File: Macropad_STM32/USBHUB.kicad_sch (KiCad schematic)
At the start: 36 parts, among them J4 USB_C_Receptacle_USB2.0, J5 USB_C_Receptacle_USB2.0, J6 USB_C_Receptacle_USB2.0, U2 CY7C65632-28LTXCT, U4 USBLC6-2SC6, U5 USBLC6-2SC6, U6 USBLC6-2SC6, U7 USBLC6-2SC6, Y1 12MHz

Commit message: Schematic changes Motherboard nearing completion
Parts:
- removed C17, C18, C19: 100n, Capacitor_SMD:C_0805_2012Metric_Pad1.18x1.45mm_HandSolder, symbol Device:C
- removed F2: 500mA, Fuse:Fuse_1206_3216Metric_Pad1.42x1.75mm_HandSolder, symbol Device:Polyfuse
- removed FB1 (x2): 600R, Fuse:Fuse_0805_2012Metric_Pad1.15x1.40mm_HandSolder, symbol Device:FerriteBead_Small
- removed J4, J5: USB_C_Receptacle_USB2.0, Connector_USB:USB_C_Receptacle_HRO_TYPE-C-31-M-12, symbol Hub16-rescue:USB_C_Receptacle_USB2.0-Connector
- removed U4, U5: USBLC6-2SC6, Package_TO_SOT_SMD:SOT-23-6, symbol Hub16-rescue:USBLC6-2SC6-josh-ic
- added C18, C37, C59: 2u2, Capacitor_SMD:C_0805_2012Metric_Pad1.18x1.45mm_HandSolder, symbol Device:C_Small
- added C19, C61, C62: 100u, Capacitor_SMD:C_Elec_6.3x5.4, symbol Device:C_Polarized
- added F5: 500mA, Fuse:Fuse_1206_3216Metric_Pad1.42x1.75mm_HandSolder, symbol Device:Polyfuse
- added FB1 (x2): 120R, Fuse:Fuse_0805_2012Metric_Pad1.15x1.40mm_HandSolder, symbol Device:FerriteBead_Small
- added J13, J14, J17, J18, J19, J5: Conn_01x04_Socket, Connector_PinHeader_2.54mm:PinHeader_1x04_P2.54mm_Vertical, symbol Connector:Conn_01x04_Socket
- added J15, J20: USB_C_Receptacle_USB2.0, Connector_USB:USB_C_Receptacle_HRO_TYPE-C-31-M-12, symbol Hub16-rescue:USB_C_Receptacle_USB2.0-Connector
- added U8: USBLC6-2SC6, Package_TO_SOT_SMD:SOT-23-6, symbol Hub16-rescue:USBLC6-2SC6-josh-ic
- FB1: value 600R -> 120R
- R10, R11, R8, R9: now not fitted
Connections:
- net +5V: now also J13.1 (Pin_1), J18.1 (Pin_1), J5.1 (Pin_1); no longer FB1.2
- net D1_D+: now also J18.3 (Pin_3), J19.3 (Pin_3), U8.4 (IO2)
- net D1_D-: now also J18.2 (Pin_2), J19.2 (Pin_2), U8.6 (IO1)
- net D2_D+: now also J17.3 (Pin_3), J5.3 (Pin_3)
- net D2_D-: now also J17.2 (Pin_2), J5.2 (Pin_2)
- net D3_D+: now also J13.3 (Pin_3), J14.3 (Pin_3)
- net D3_D-: now also J13.2 (Pin_2), J14.2 (Pin_2)
- net GND: now also C18.2, C19.2, C37.2, C59.2, C61.2, C62.2, J13.4 (Pin_4), J18.4 (Pin_4), J5.4 (Pin_4); no longer J6.A1 (GND), J6.A12 (GND), J6.B1 (GND), J6.B12 (GND), J6.S1 (SHIELD), U6.2 (GND), U7.2 (GND)
- net D3_VBUS: now reaches F4.1, J6.A4 (VBUS), J6.A9 (VBUS), J6.B4 (VBUS), J6.B9 (VBUS), U7.5 (VBUS)
- net at F4.2, FB1.1: now also C62.1
- net at U6.1 (IO1): now also J15.A7 (D-), J15.B7 (D-)
- net at U6.3 (IO2): now also J15.A6 (D+), J15.B6 (D+)
- net D1_VBUS: now reaches F3.1
- net D1_VBUS: now also J20.A4 (VBUS), J20.A9 (VBUS), J20.B4 (VBUS), J20.B9 (VBUS), U8.5 (VBUS); no longer U6.5 (VBUS)
- net at F3.2: now also C61.1, FB1.1
- new net: C19.1, F5.2, FB1.1
- new net: C18.1, FB1.2, J17.1 (Pin_1)
- new net: C59.1, FB1.2, J14.1 (Pin_1)
- new net: J20.A6 (D+), J20.B6 (D+), U8.3 (IO2)
- new net: J20.A7 (D-), J20.B7 (D-), U8.1 (IO1)
- new net: C37.1, FB1.2, J19.1 (Pin_1)
- new net D1_GND: J19.4 (Pin_4), J20.A1 (GND), J20.A12 (GND), J20.B1 (GND), J20.B12 (GND), J20.S1 (SHIELD), U8.2 (GND)
- new net D2_GND: J15.A1 (GND), J15.A12 (GND), J15.B1 (GND), J15.B12 (GND), J15.S1 (SHIELD), J17.4 (Pin_4), U6.2 (GND)
- new net D2_VBUS: F5.1, J15.A4 (VBUS), J15.A9 (VBUS), J15.B4 (VBUS), J15.B9 (VBUS), U6.5 (VBUS)
- new net D3_GND: J14.4 (Pin_4), J6.A1 (GND), J6.A12 (GND), J6.B1 (GND), J6.B12 (GND), J6.S1 (SHIELD), U7.2 (GND)
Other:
- company: (none) -> Irfaan
- title: (none) -> STM32 Macropad
- moved on the sheet: C27, C28, F4, FB1, JP2, R12, R13, U2, U7, Y1

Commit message: Revision 1 nearly finished
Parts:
- removed J15, J20: USB_C_Receptacle_USB2.0, Connector_USB:USB_C_Receptacle_HRO_TYPE-C-31-M-12, symbol Hub16-rescue:USB_C_Receptacle_USB2.0-Connector
- added J2, J8: USB_A, SK6812SIDE:AMPHENOL_UE27AC54100, symbol Connector:USB_A
- J13, J14, J17, J18, J19, J5: footprint Connector_PinHeader_2.54mm:PinHeader_1x04_P2.54mm_Vertical -> SK6812SIDE:MOLEX_0781710004
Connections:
- net +3V3 is gone; now on net +3.3V: C27.1, C28.1
- net D1_D+: no longer J19.3 (Pin_3), U8.4 (IO2)
- net D1_D-: no longer J19.2 (Pin_2), U8.6 (IO1)
- net D1_GND: now also C37.2, C61.2, J2.4 (GND), J2.5 (Shield)
- net D1_VBUS: now also J2.1 (VBUS)
- net D2_D+: no longer J17.3 (Pin_3), U6.4 (IO2)
- net D2_D-: no longer J17.2 (Pin_2), U6.6 (IO1)
- net D2_GND: now also C18.2, C19.2, J8.4 (GND), J8.5 (Shield)
- net D2_VBUS: now also J8.1 (VBUS)
- net D3_D+: no longer J14.3 (Pin_3), U7.4 (IO2)
- net D3_D-: no longer J14.2 (Pin_2), U7.6 (IO1)
- net D3_GND: now also C59.2, C62.2
- net GND: no longer C18.2, C19.2, C37.2, C59.2, C61.2, C62.2
- net at U8.3 (IO2): now also J2.3 (D+)
- net at U8.1 (IO1): now also J2.2 (D-)
- net at U6.1 (IO1): now also J8.2 (D-)
- net at U6.3 (IO2): now also J8.3 (D+)
- new net Daughter_D1_D+: J19.3 (Pin_3), U8.4 (IO2)
- new net Daughter_D1_D-: J19.2 (Pin_2), U8.6 (IO1)
- new net Daughter_D2_D+: J17.3 (Pin_3), U6.4 (IO2)
- new net Daughter_D2_D-: J17.2 (Pin_2), U6.6 (IO1)
- new net Daughter_D3_D+: J14.3 (Pin_3), U7.4 (IO2)
- new net Daughter_D3_D-: J14.2 (Pin_2), U7.6 (IO1)
- no-connect marks 15 -> 7

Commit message: Nearly finished Todo: - Fix silkscreen - Final check
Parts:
- removed J13, J14, J17, J18, J19, J5: Conn_01x04_Socket, SK6812SIDE:MOLEX_0781710004, symbol Connector:Conn_01x04_Socket
- JP2: footprint Connector_PinHeader_2.54mm:PinHeader_1x03_P2.54mm_Vertical -> Jumper:SolderJumper-3_P2.0mm_Open_TrianglePad1.0x1.5mm_NumberLabels
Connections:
- net D1_GND is gone; now on net GND: C37.2, C61.2, J2.4 (GND), J2.5 (Shield), U8.2 (GND)
- net D1_VBUS is gone; now on net +5V: F3.1, J2.1 (VBUS), U8.5 (VBUS)
- net D2_GND is gone; now on net GND: C18.2, C19.2, J8.4 (GND), J8.5 (Shield), U6.2 (GND)
- net D2_VBUS is gone; now on net +5V: F5.1, J8.1 (VBUS), U6.5 (VBUS)
- net D3_GND is gone; now on net GND: C59.2, C62.2, J6.A1 (GND), J6.A12 (GND), J6.B1 (GND), J6.B12 (GND), J6.S1 (SHIELD), U7.2 (GND)
- net D3_VBUS is gone; now on net +5V: F4.1, J6.A4 (VBUS), J6.A9 (VBUS), J6.B4 (VBUS), J6.B9 (VBUS), U7.5 (VBUS)
- net Daughter_D1_D+ is gone; now on net D2_D+: U8.4 (IO2)
- net Daughter_D1_D- is gone; now on net D2_D-: U8.6 (IO1)
- net Daughter_D2_D+ is gone; now on net D3_D+: U6.4 (IO2)
- net Daughter_D2_D- is gone; now on net D3_D-: U6.6 (IO1)
- net Daughter_D3_D+ is gone; now on net D1_D+: U7.4 (IO2)
- net Daughter_D3_D- is gone; now on net D1_D-: U7.6 (IO1)
- net +5V: now also C18.1, C37.1, C59.1, FB1.2, FB1.2, FB1.2

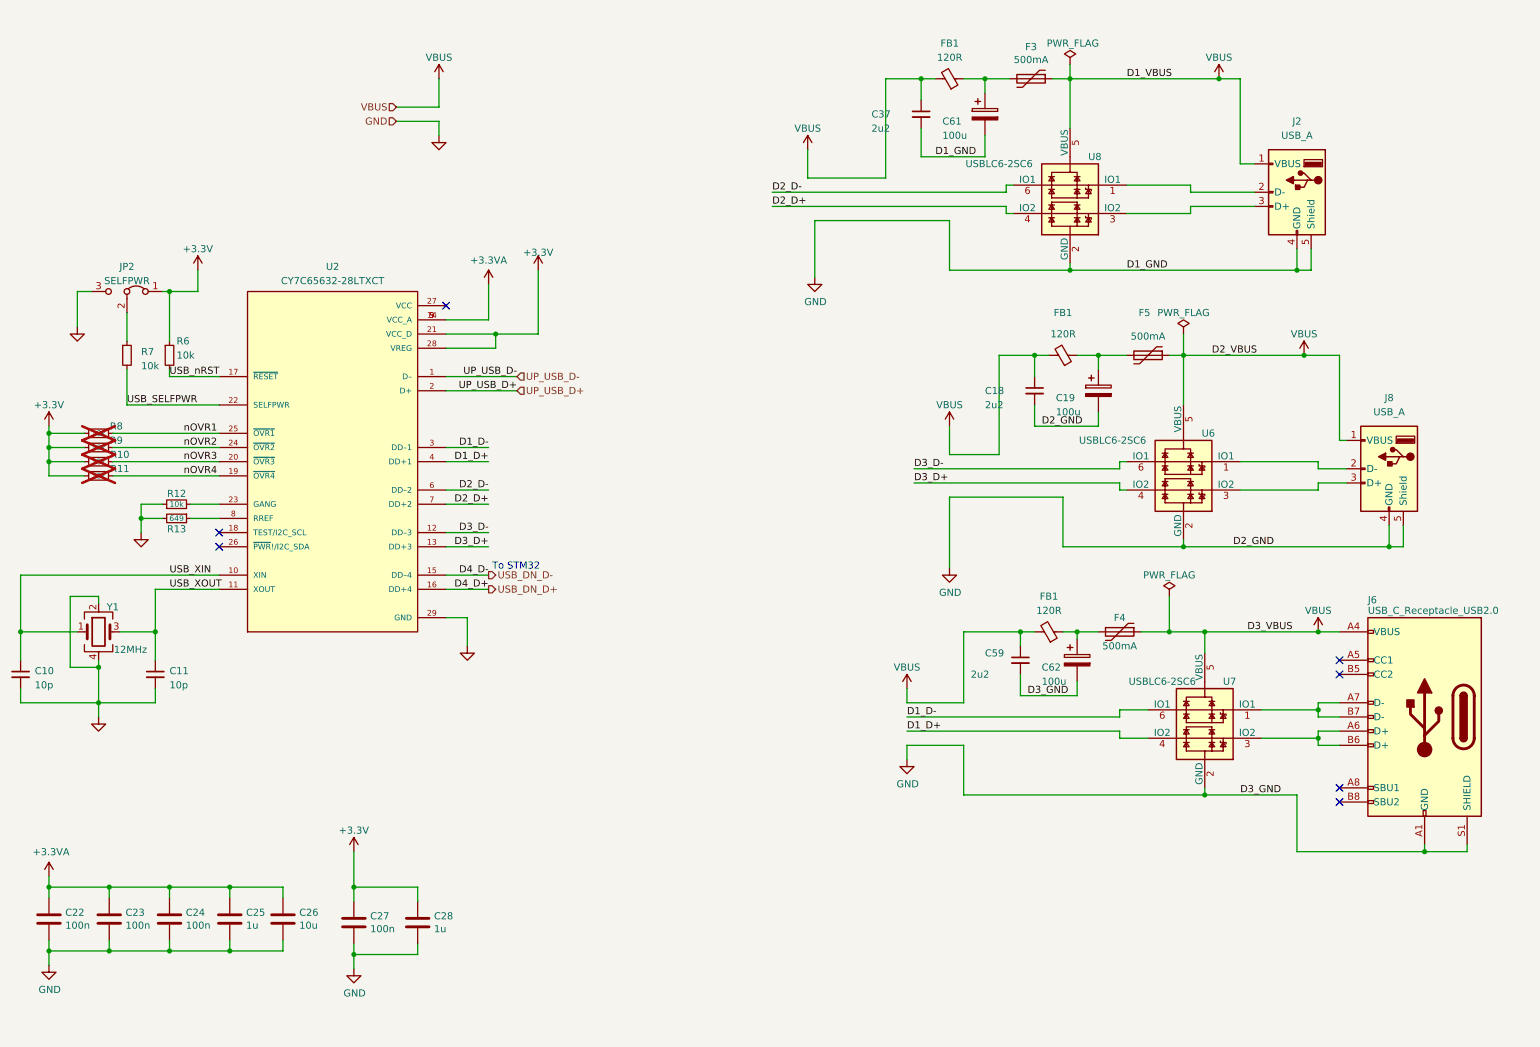
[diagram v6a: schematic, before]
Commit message: Hardware finished and motherboard has been tested. Todo: Test keyboard matrix and write firmware.
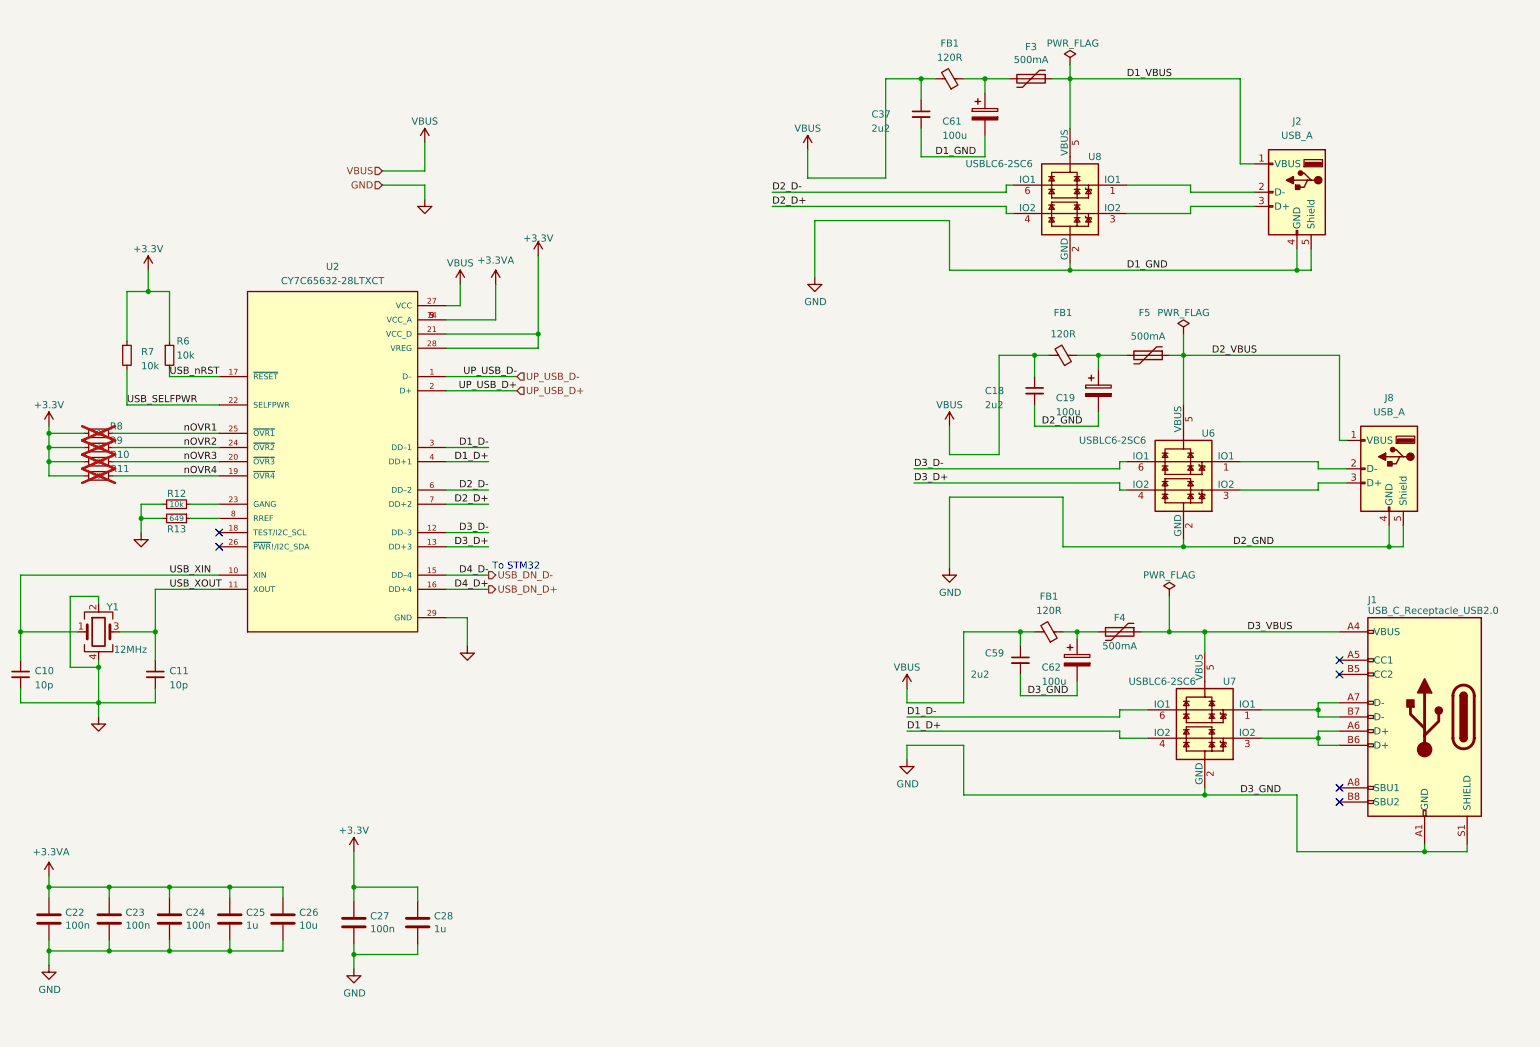
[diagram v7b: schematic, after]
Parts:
- removed JP2: SELFPWR, Jumper:SolderJumper-3_P2.0mm_Open_TrianglePad1.0x1.5mm_NumberLabels, symbol Jumper:Jumper_3_Bridged12
- renumbered J6 to J1
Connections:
- net +3.3V: now also R7.1
- net +5V: now also U2.27 (VCC); no longer F3.1, F4.1, F5.1, J1.A4 (VBUS), J1.A9 (VBUS), J1.B4 (VBUS), J1.B9 (VBUS), J2.1 (VBUS), J8.1 (VBUS), U6.5 (VBUS), U7.5 (VBUS), U8.5 (VBUS)
- new net D1_VBUS: F3.1, J2.1 (VBUS), U8.5 (VBUS)
- new net D2_VBUS: F5.1, J8.1 (VBUS), U6.5 (VBUS)
- new net D3_VBUS: F4.1, J1.A4 (VBUS), J1.A9 (VBUS), J1.B4 (VBUS), J1.B9 (VBUS), U7.5 (VBUS)
- no-connect marks 7 -> 6
